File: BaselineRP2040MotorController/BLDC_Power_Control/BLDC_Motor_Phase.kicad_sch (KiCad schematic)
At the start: 28 parts, among them Q3 Q_PNP_BEC, U10 INA240A1D, U9 EG3113

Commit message: Change Mosfet Footprint.
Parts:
- AH3: footprint fdsaafds -> [EastMakes] Mosfets:PowerPAK_SO-8_123
- AL3: footprint afddaffdaafds -> [EastMakes] Mosfets:PowerPAK_SO-8_123
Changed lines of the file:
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@@
 			(effects
 				(font
-					(size 0.001 0.001)
+					(size 0.0254 0.0254)
 				)
 				(hide yes)
@@
 			(effects
 				(font
-					(size 0.001 0.001)
+					(size 0.0254 0.0254)
 				)
 				(hide yes)
@@
 			)
 		)
-		(property "Footprint" "fdsaafds"
+		(property "Footprint" "[EastMakes] Mosfets:PowerPAK_SO-8_123"
 			(at 143.51 55.88 0)
 			(effects
@@
 			)
 		)
-		(property "Footprint" "afddaffdaafds"
+		(property "Footprint" "[EastMakes] Mosfets:PowerPAK_SO-8_123"
 			(at 152.4 71.12 0)
 			(effects

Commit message: Erhhhhrh
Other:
- moved on the sheet: C28, C29, C30, C31, C32, C33, D10, D11, D12, D13, Q3, R36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

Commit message: Generate PDF
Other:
- title: (none) -> BLDC Starting Point
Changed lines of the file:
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@@
 	(generator_version "8.0")
 	(paper "A5")
+	(title_block
+		(title "BLDC Starting Point")
+		(comment 1 "Florian, Josh and EMF Group Release")
+	)
 	(junction
 		(at 50.8 50.8)

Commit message: Post Feedback Changes.
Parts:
- added C1: 0, Capacitor_SMD:C_0603_1608Metric, symbol Device:C
- added R1: 0Ω, Resistor_SMD:R_2512_6332Metric, symbol MotorController:TAYLOR_RESISTOR
- Q3, R41, R44: now not fitted
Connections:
- net ${PhaseDesignator}_SENSE: now also C1.2, R1.1; no longer U10.5
- net GND: now also C1.1
- new net: R1.2, U10.5
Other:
- note added: "Current Sense Filter"
- note added: "Flagged as Questionable Not in the reference design. But used upstream by Twisted Fields, so now marked as DNP"
- note added: "Populate Later If Needed"
- moved on the sheet: C28, C29, C30, C31, C32, C33, D10, D11, D12, D13, R36, R37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

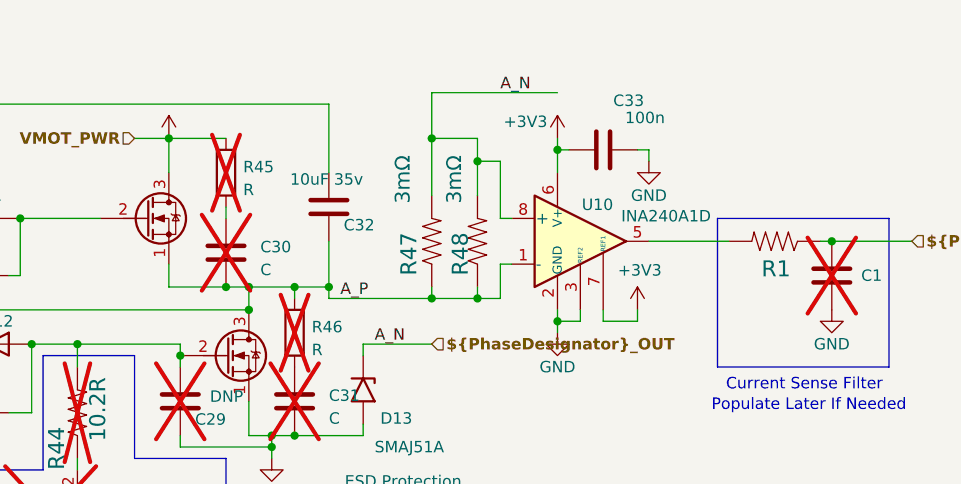
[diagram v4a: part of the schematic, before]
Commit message: Should have been a 4 layer board.
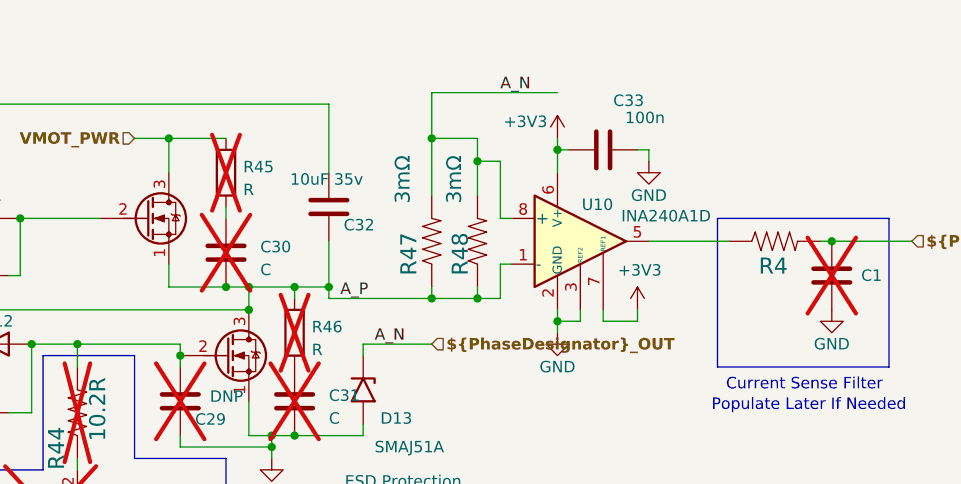
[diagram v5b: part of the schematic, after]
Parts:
- removed R1: 0Ω, Resistor_SMD:R_2512_6332Metric, symbol MotorController:TAYLOR_RESISTOR
- added R4: 0, Resistor_SMD:R_0603_1608Metric, symbol MotorController:TAYLOR_RESISTOR
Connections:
- net ${PhaseDesignator}_SENSE: now also R4.2
- net at U10.5: now also R4.1
- net VMOT renamed VMOT_PWR
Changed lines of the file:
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@@
+	(symbol
+		(lib_id "MotorController:TAYLOR_RESISTOR")
+		(at 167.64 50.8 0)
+		(unit 1)
+		(exclude_from_sim no)
+		(in_bom yes)
+		(on_board yes)
+		(dnp no)
+		(property "Reference" "R4"
+			(at 165.862 54.61 0)
+			(effects
+				(font
+					(size 1.778 1.778)
+				)
+				(justify left bottom)
+			)
+		)
+		(property "Value" "0"
+			(at 163.83 54.102 0)
+			(effects
+				(font
+					(size 1.778 1.778)
+				)
+				(justify left bottom)
+				(hide yes)
+			)
+		)
+		(property "Footprint" "Resistor_SMD:R_0603_1608Metric"
+			(at 167.64 50.8 0)
+			(effects
+				(font
+					(size 1.27 1.27)
+				)
+				(hide yes)
+			)
+		)
+		(property "Datasheet" ""
+			(at 167.64 50.8 0)
+			(effects
+				(font
+					(size 1.27 1.27)
+				)
+				(hide yes)
+			)
+		)
+		(property "Description" ""
+			(at 167.64 50.8 0)
+			(effects
+				(font
+					(size 1.27 1.27)
+				)
+				(hide yes)
+			)
+		)
+		(property "LCSC" "C2933129"
+			(at 167.64 50.8 0)
+			(effects
+				(font
+					(size 1.27 1.27)
+				)
+				(hide yes)
+			)
+		)
+		(pin "1"
+		)
+		(pin "2"
+		)
+		(instances
+			(project "BaselineRP2040MotorController"
+				(path "/085e5f08-c826-4caa-b8e2-0a741609456e/adfc6ecc-6038-43a2-a2be-baacb83b86f1/70bbc80f-daaf-419a-a8c6-d63d9a60e08e"
+					(reference "R4")
+					(unit 1)
+				)
+				(path "/085e5f08-c826-4caa-b8e2-0a741609456e/adfc6ecc-6038-43a2-a2be-baacb83b86f1/c18ba0a7-96c1-4e03-8f0f-e6aa1a6bfcf5"
+					(reference "R5")
+					(unit 1)
+				)
+				(path "/085e5f08-c826-4caa-b8e2-0a741609456e/adfc6ecc-6038-43a2-a2be-baacb83b86f1/5464c955-cdc3-44b9-a505-ba7a9b088c6c"
+					(reference "R6")
+					(unit 1)
+				)
+			)
+		)
+	)
 	(symbol
 		(lib_id "MotorController:TAYLOR_RESISTOR")
@@
 	)
 	(symbol
-		(lib_id "MotorBuck:VMOT")
-		(at 100.33 39.37 0)
-		(unit 1)
-		(exclude_from_sim no)
-		(in_bom yes)
-		(on_board yes)
-		(dnp no)
-		(property "Reference" "#PWR062"
-			(at 100.33 43.18 0)
-			(effects
-				(font
-					(size 1.27 1.27)
-				)
-				(hide yes)
-			)
-		)
-		(property "Value" "VMOT"
-			(at 96.52 36.83 0)
-			(effects
-				(font
-					(size 1.27 1.27)
-				)
-				(hide yes)
-			)
-		)
-		(property "Footprint" ""
-			(at 100.33 39.37 0)
-			(effects
-				(font
-					(size 1.27 1.27)
-				)
-				(hide yes)
-			)
-		)
-		(property "Datasheet" ""
-			(at 100.33 39.37 0)
-			(effects
-				(font
-					(size 1.27 1.27)
-				)
-				(hide yes)
-			)
-		)
-		(property "Description" ""
-			(at 100.33 39.37 0)
-			(effects
-				(font
-					(size 1.27 1.27)
-				)
-				(hide yes)
-			)
-		)
-		(property "Sim.Device" "SPICE"
-			(at 100.33 43.18 0)
-			(effects
-				(font
-					(size 1.27 1.27)
-				)
-				(hide yes)
-			)
-		)
-		(property "Sim.Params" "type=\"I\" model=\"VMOT\" lib=\"\""
-			(at -275.59 -95.885 0)
-			(effects
-				(font
-					(size 0.0254 0.0254)
-				)
-				(hide yes)
-			)
-		)
-		(property "Sim.Pins" "1=1"
-			(at -275.59 -95.885 0)
-			(effects
-				(font
-					(size 0.0254 0.0254)
-				)
-				(hide yes)
-			)
-		)
-		(pin "1"
-		)
-		(instances
-			(project "BaselineRP2040MotorController"
-				(path "/085e5f08-c826-4caa-b8e2-0a741609456e/adfc6ecc-6038-43a2-a2be-baacb83b86f1/5464c955-cdc3-44b9-a505-ba7a9b088c6c"
-					(reference "#PWR062")
-					(unit 1)
-				)
-				(path "/085e5f08-c826-4caa-b8e2-0a741609456e/adfc6ecc-6038-43a2-a2be-baacb83b86f1/70bbc80f-daaf-419a-a8c6-d63d9a60e08e"
-					(reference "#PWR038")
-					(unit 1)
-				)
-				(path "/085e5f08-c826-4caa-b8e2-0a741609456e/adfc6ecc-6038-43a2-a2be-baacb83b86f1/c18ba0a7-96c1-4e03-8f0f-e6aa1a6bfcf5"
-					(reference "#PWR050")
-					(unit 1)
-				)
-			)
-		)
-	)
-	(symbol
 		(lib_id "power:GND")
 		(at 26.67 52.07 0)
@@
 					(unit 1)
 				)
-			)
-		)
-	)
-	(symbol
-		(lib_id "MotorController:TAYLOR_RESISTOR")
-		(at 167.64 50.8 180)
-		(unit 1)
-		(exclude_from_sim no)
-		(in_bom yes)
-		(on_board yes)
-		(dnp no)
-		(property "Reference" "R1"
-			(at 169.418 52.832 0)
-			(effects
-				(font
-					(size 1.778 1.778)
-				)
-				(justify left bottom)
-			)
-		)
-		(property "Value" "0Ω"
-			(at 165.608 53.848 0)
-			(effects
-				(font
-					(size 1.651 1.651)
-				)
-				(justify left top)
-				(hide yes)
-			)
-		)
-		(property "Footprint" "Resistor_SMD:R_2512_6332Metric"
-			(at 167.64 50.8 0)
-			(effects
-				(font
-					(size 1.27 1.27)
-				)
-				(hide yes)
-			)
-		)
-		(property "Datasheet" ""
-			(at 167.64 50.8 0)
-			(effects
-				(font
-					(size 1.27 1.27)
-				)
-				(hide yes)
-			)
-		)
-		(property "Description" ""
-			(at 167.64 50.8 0)
-			(effects
-				(font
-					(size 1.27 1.27)
-				)
-				(hide yes)
-			)
-		)
-		(property "LCSC" "C2688862"
-			(at 167.64 50.8 0)
-			(effects
-				(font
-					(size 1.27 1.27)
-				)
-				(hide yes)
-			)
-		)
-		(pin "1"
-		)
-		(pin "2"
-		)
-		(instances
-			(project "BaselineRP2040MotorController"
-				(path "/085e5f08-c826-4caa-b8e2-0a741609456e/adfc6ecc-6038-43a2-a2be-baacb83b86f1/70bbc80f-daaf-419a-a8c6-d63d9a60e08e"
-					(reference "R1")
-					(unit 1)
-				)
-				(path "/085e5f08-c826-4caa-b8e2-0a741609456e/adfc6ecc-6038-43a2-a2be-baacb83b86f1/c18ba0a7-96c1-4e03-8f0f-e6aa1a6bfcf5"
-					(reference "R2")
-					(unit 1)
-				)
-				(path "/085e5f08-c826-4caa-b8e2-0a741609456e/adfc6ecc-6038-43a2-a2be-baacb83b86f1/5464c955-cdc3-44b9-a505-ba7a9b088c6c"
-					(reference "R3")
-					(unit 1)
-				)

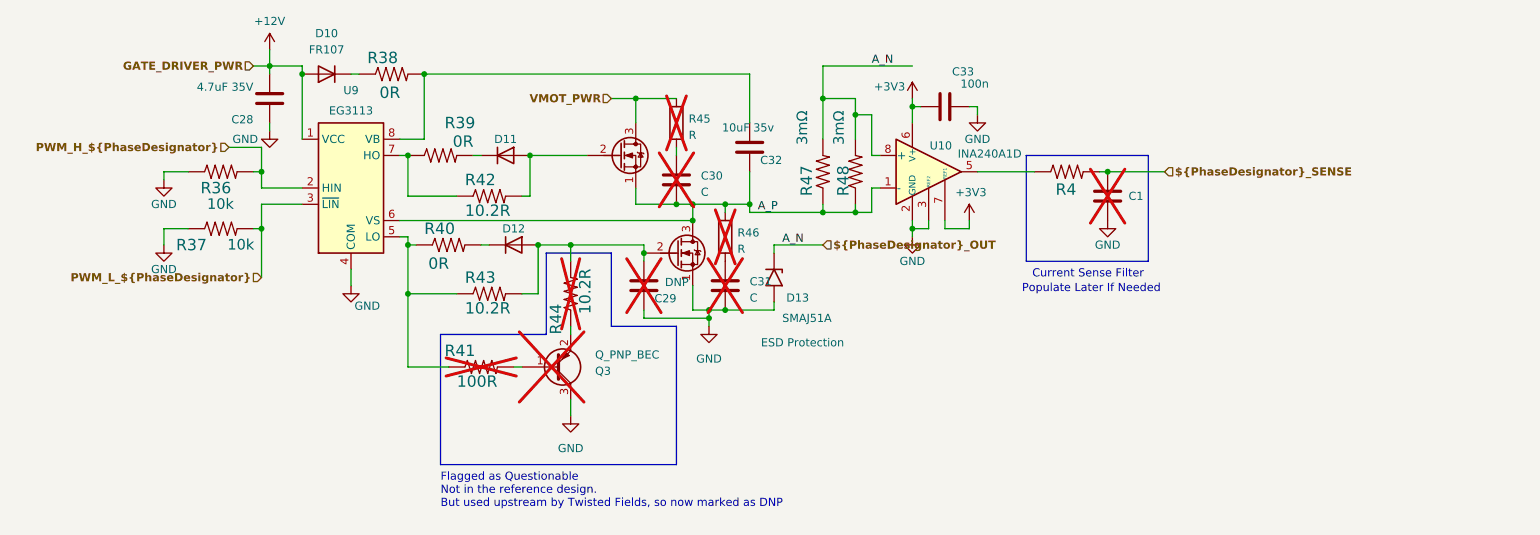
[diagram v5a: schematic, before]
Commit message: Make a cut down board.
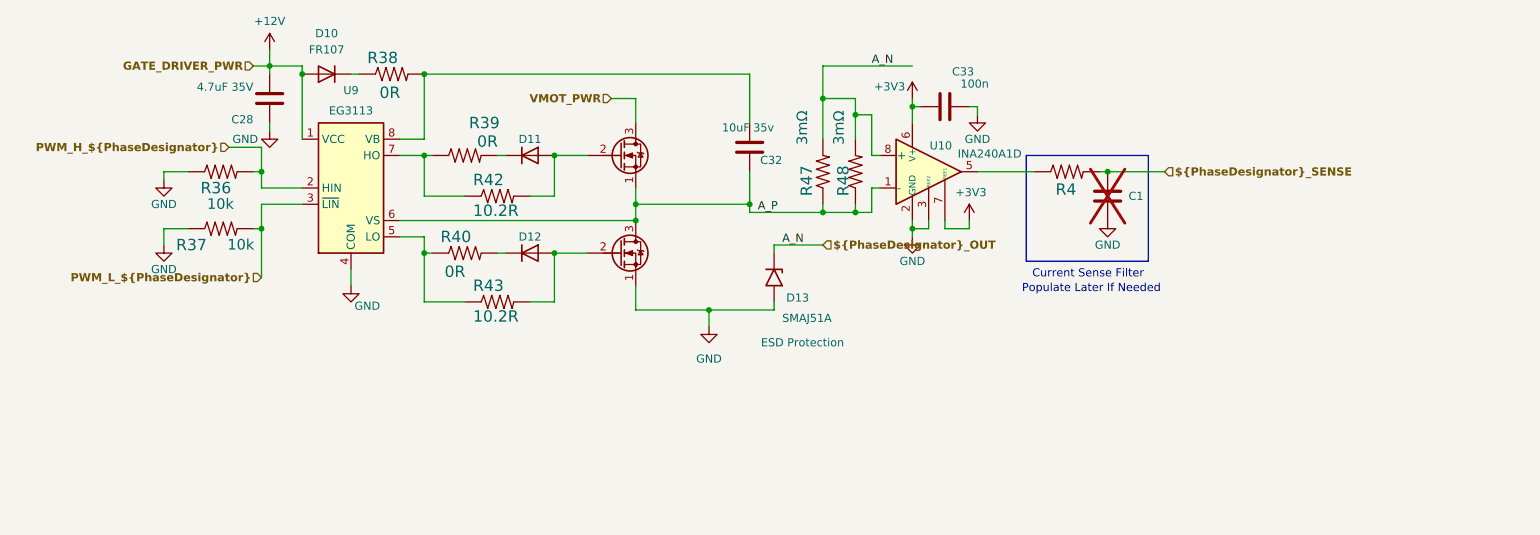
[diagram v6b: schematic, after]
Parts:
- removed C29: DNP, Capacitor_SMD:C_0603_1608Metric, symbol Device:C
- removed C30, C31: C, Capacitor_SMD:C_0805_2012Metric, symbol Device:C
- removed Q3: Q_PNP_BEC, Package_TO_SOT_SMD:SOT-23, symbol Device:Q_PNP_BEC
- removed R41: 100R, Resistor_SMD:R_0603_1608Metric, symbol MotorController:TAYLOR_RESISTOR
- removed R44: 10.2R, Resistor_SMD:R_0603_1608Metric, symbol MotorController:TAYLOR_RESISTOR
- removed R45, R46: R, Resistor_SMD:R_0805_2012Metric, symbol Device:R
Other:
- note removed: "Flagged as Questionable Not in the reference design. But used upstream by Twisted Fields, so now marked as DNP"
- moved on the sheet: D11, D12, R39, R40, R42, R43
